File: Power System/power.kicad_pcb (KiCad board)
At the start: 2 copper layers, 139.7 x 100.3 mm, 35 parts, among them J1 PC104_40Pin_2.54mm, J2 Charge Cable, J3 Battery Pack, J4 IDC Header, U1 ds2781e+

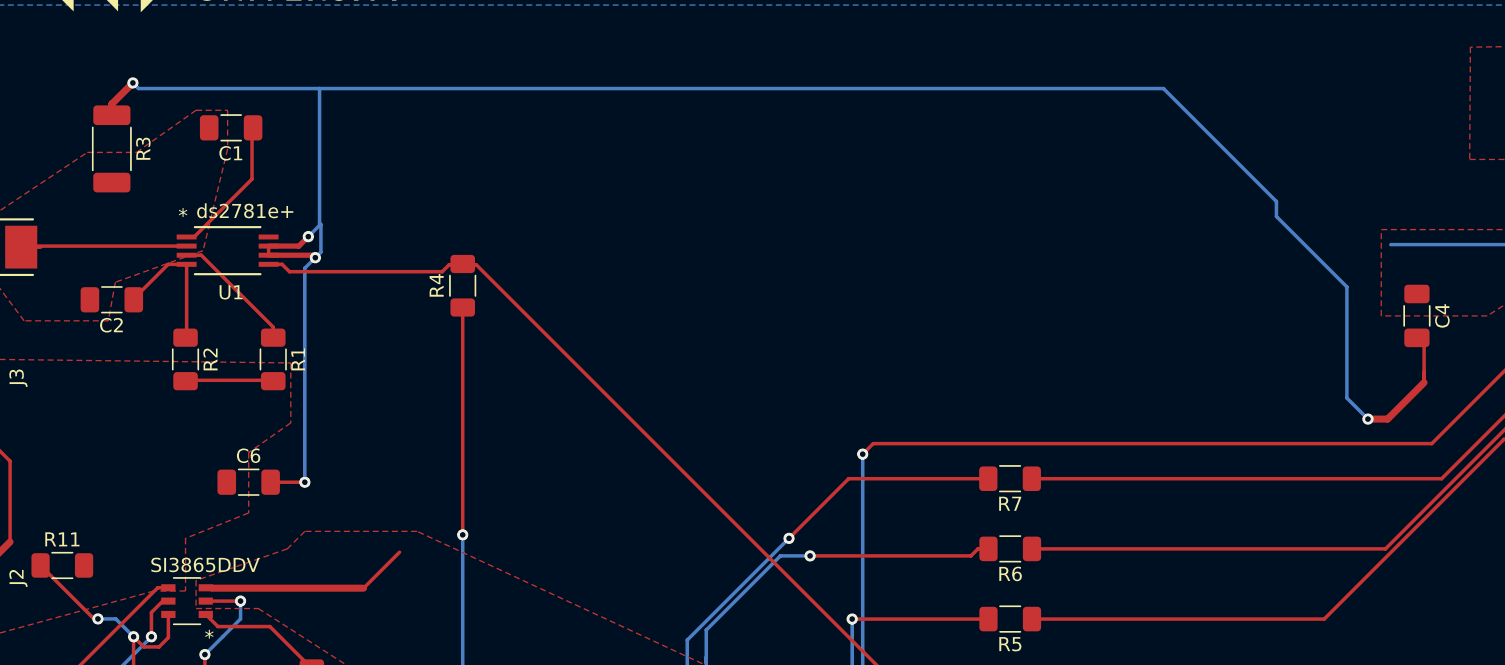
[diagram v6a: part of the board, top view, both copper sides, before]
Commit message: Tried routing things using recommendations. Late though- may be unideal...
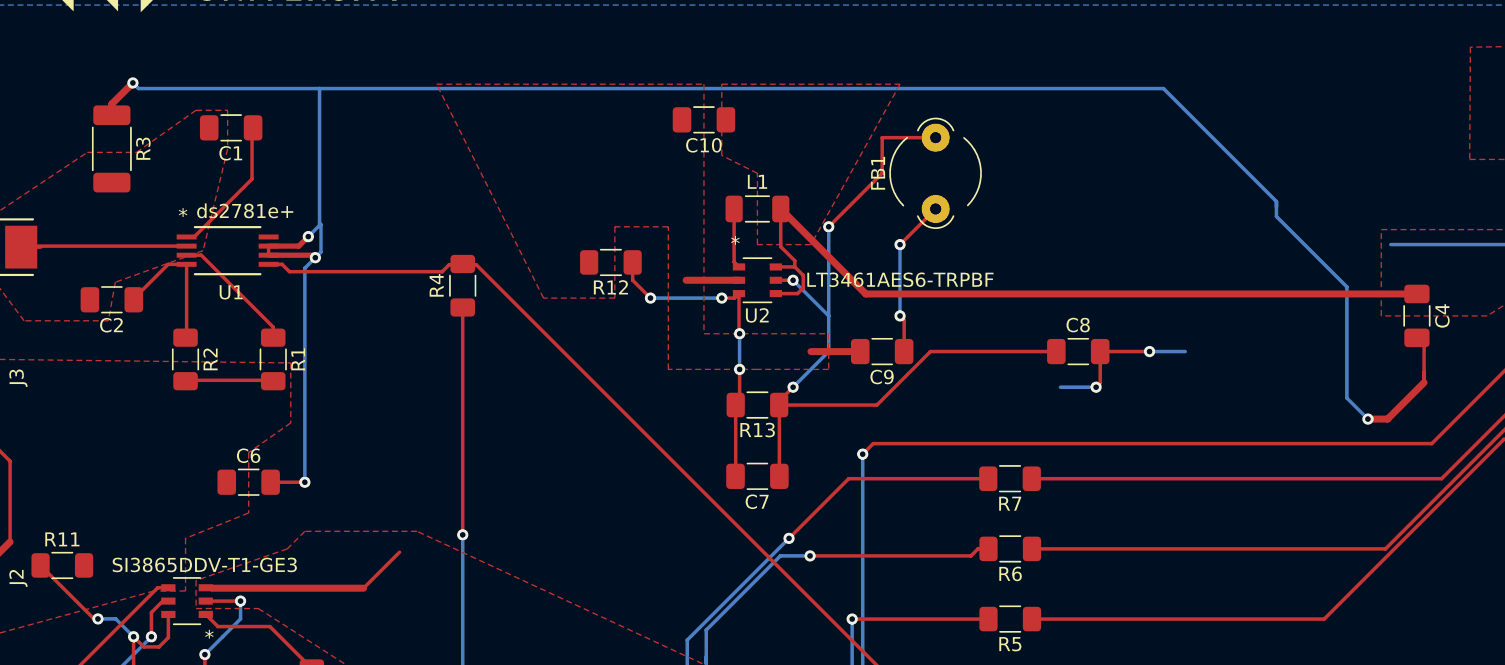
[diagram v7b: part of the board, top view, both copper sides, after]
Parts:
- added C10: 1uF, Capacitor_SMD:C_1206_3216Metric_Pad1.33x1.80mm_HandSolder, F.Cu at (91.4, 43.2)
- added C7: 22pF, Capacitor_SMD:C_1206_3216Metric_Pad1.33x1.80mm_HandSolder, F.Cu at (95.2, 68.6)
- added C8: 0.47uF, Capacitor_SMD:C_1206_3216Metric_Pad1.33x1.80mm_HandSolder, F.Cu at (118.1, 59.7)
- added C9: 1uF, Capacitor_SMD:C_1206_3216Metric_Pad1.33x1.80mm_HandSolder, F.Cu at (104.1, 59.7)
- added FB1: 2.5k Ferrite Bead, Ferrite_THT:LairdTech_28C0236-0JW-10, F.Cu at (108.0, 49.5)
- added L1: 47uH, Inductor_SMD:L_1206_3216Metric_Pad1.22x1.90mm_HandSolder, F.Cu at (95.2, 49.5)
- added R12: 10k, Resistor_SMD:R_1206_3216Metric_Pad1.30x1.75mm_HandSolder, F.Cu at (84.8, 53.3)
- added R13: 243k, Resistor_SMD:R_1206_3216Metric_Pad1.30x1.75mm_HandSolder, F.Cu at (95.2, 63.5)
- added U2: LT3461AES6-TRPBF, LT3461AES6-TRPBF:LT3461AES6-TRPBF, F.Cu at (95.2, 54.6)
- MOSFET1: value SI3865DDV -> SI3865DDV-T1-GE3
- R2: value 500 -> 499
- R5: value 220 -> 3.4
- R6: value 220 -> 5.1
- R7: value 220 -> 66.5
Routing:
- net +5V: track 7.62 -> 65.2 mm
- net Net-(C7-Pad1): track 0.00 -> 57.1 mm, vias 0 -> 3
- net Net-(C7-Pad2): track 0.00 -> 22.7 mm, vias 0 -> 4
- net GND: track 394.3 -> 413.7 mm, vias 8 -> 10
- net /SIPM_Power: track 0.00 -> 11.3 mm, vias 0 -> 2
- net Net-(L1-Pad1): track 0.00 -> 4.27 mm
- added copper zone on F.Cu, net GND

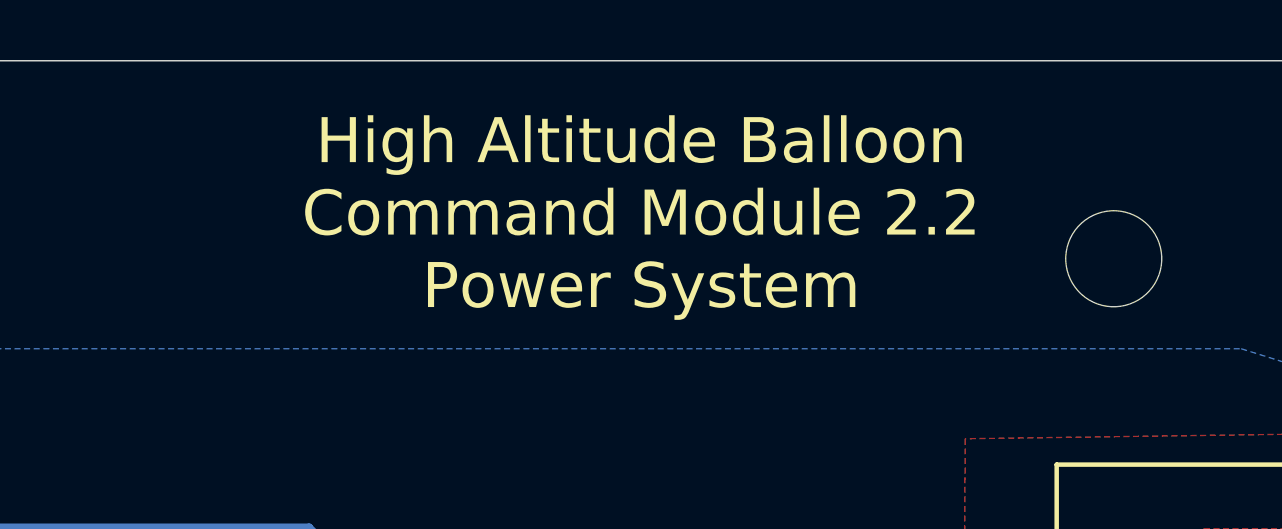
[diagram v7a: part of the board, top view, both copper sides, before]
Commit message: Changed text on board to say WhitSat instead of High Altitude Balloon Command Module 2
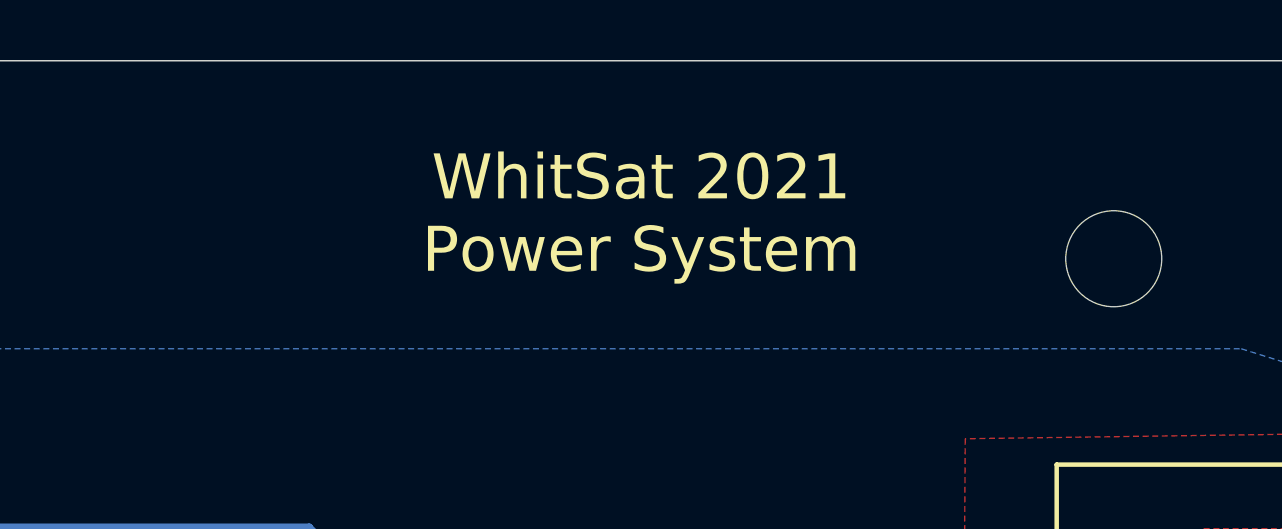
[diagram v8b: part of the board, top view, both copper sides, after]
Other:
- board text added: "WhitSat 2021 Power System"
- board text removed: "High Altitude Balloon Command Module 2.2 Power System"
